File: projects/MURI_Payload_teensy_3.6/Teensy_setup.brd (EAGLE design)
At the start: 100 x 80 mm, 52 parts, among them IC1 DS18B20, IC2 DS18B20, IC4 DS18B20, IC5 DS18B20, U2 MS560702BA03-50

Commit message: Added edits to teensy 3.6 schematic for the plantower. Added stuff from EAGLE intro presentation.
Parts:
- added B1: SPARKFUN_LOGIC_LEVEL_CONVERTER, SparkFun-Boards:SPARKFUN_LOGIC_LEVEL_CONVERTER
- added PLANTOWER: (no value), SparkFun-Connectors:1X08
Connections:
- new net TX_PT_HIGH: B1.HV1, U$1.0/RX
- new net TX_PT_LOW: B1.LV1, PLANTOWER.4
- net 5V2: now also B1.HV
- net GND: now also B1.GND1, B1.GND2, PLANTOWER.2
- net VCC: now also B1.LV, PLANTOWER.1
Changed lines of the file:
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@@
 <attribute name="VALUE" x="-81.6356" y="-9.3726" size="0.9906" layer="27" ratio="10"/>
+</element>
+<element name="B1" library="SparkFun-Boards" library_urn="urn:adsk.eagle:library:509" package="SPARKFUN_LOGIC_LEVEL_CONVERTER" package3d_urn="urn:adsk.eagle:package:37318/1" value="SPARKFUN_LOGIC_LEVEL_CONVERTER" x="-91.44" y="-1.27" smashed="yes">
+<attribute name="NAME" x="-91.44" y="6.604" size="0.6096" layer="25" font="vector" ratio="20" align="bottom-center"/>
+<attribute name="VALUE" x="-91.44" y="-9.144" size="0.6096" layer="25" font="vector" ratio="20" align="top-center"/>
+</element>
+<element name="PLANTOWER" library="SparkFun-Connectors" library_urn="urn:adsk.eagle:library:513" package="1X08" package3d_urn="urn:adsk.eagle:package:38138/1" value="" x="-96.52" y="-12.7" smashed="yes">
+<attribute name="NAME" x="-97.79" y="-11.303" size="0.6096" layer="25" font="vector" ratio="20"/>
+<attribute name="PROD_ID" value="CONN-08438" x="-96.52" y="-12.7" size="1.778" layer="27" display="off"/>
+<attribute name="VALUE" x="-97.79" y="-14.732" size="0.6096" layer="27" font="vector" ratio="20"/>
 </element>
 </elements>
@@
 <contactref element="UBLOX" pad="4"/>
 <contactref element="XBEE" pad="4"/>
+<contactref element="PLANTOWER" pad="2"/>
+<contactref element="B1" pad="GND1"/>
+<contactref element="B1" pad="GND2"/>
+<wire x1="-96.52" y1="-2.54" x2="-93.98" y2="-12.7" width="0" layer="19" extent="1-1"/>
+<wire x1="-86.36" y1="-2.54" x2="-96.52" y2="-2.54" width="0" layer="19" extent="1-1"/>
+<wire x1="-73.66" y1="2.54" x2="-86.36" y2="-2.54" width="0" layer="19" extent="1-1"/>
 <wire x1="-80.01" y1="24.13" x2="-73.66" y2="2.54" width="0" layer="19" extent="1-1"/>
 <wire x1="-71.12" y1="38.1" x2="-80.01" y2="24.13" width="0" layer="19" extent="1-1"/>
@@
 <contactref element="BATTERY_HEATER_RELAY" pad="6"/>
 <contactref element="BATTERY_HEATER_RELAY" pad="9"/>
+<contactref element="B1" pad="HV"/>
+<wire x1="-69.85" y1="21.6154" x2="-86.36" y2="0" width="0" layer="19" extent="1-1"/>
 <wire x1="-64.77" y1="26.6954" x2="-69.85" y2="21.6154" width="0" layer="19" extent="1-1"/>
 <wire x1="-57.15" y1="21.6154" x2="-64.77" y2="26.6954" width="0" layer="19" extent="1-1"/>
@@
 <contactref element="R11" pad="2"/>
 <contactref element="U2" pad="2"/>
+<contactref element="PLANTOWER" pad="1"/>
+<contactref element="B1" pad="LV"/>
+<wire x1="-96.52" y1="0" x2="-96.52" y2="-12.7" width="0" layer="19" extent="1-1"/>
+<wire x1="-76.2" y1="-8.89" x2="-96.52" y2="-12.7" width="0" layer="19" extent="1-1"/>
 <wire x1="-76.2" y1="-3.81" x2="-76.2" y2="-8.89" width="0" layer="19" extent="1-1"/>
 <wire x1="-68.58" y1="17.78" x2="-76.2" y2="-3.81" width="0" layer="19" extent="1-1"/>
@@
 <wire x1="-15.24" y1="17.78" x2="-50.8" y2="63.5" width="0" layer="19" extent="1-1"/>
 </signal>
+<signal name="TX_PT_HIGH">
+<contactref element="B1" pad="HV1"/>
+<contactref element="U$1" pad="0/RX"/>
+<wire x1="-71.12" y1="2.54" x2="-86.36" y2="5.08" width="0" layer="19" extent="1-1"/>
+</signal>
+<signal name="TX_PT_LOW">
+<contactref element="B1" pad="LV1"/>
+<contactref element="PLANTOWER" pad="4"/>
+<wire x1="-96.52" y1="5.08" x2="-88.9" y2="-12.7" width="0" layer="19" extent="1-1"/>
+</signal>
 </signals>

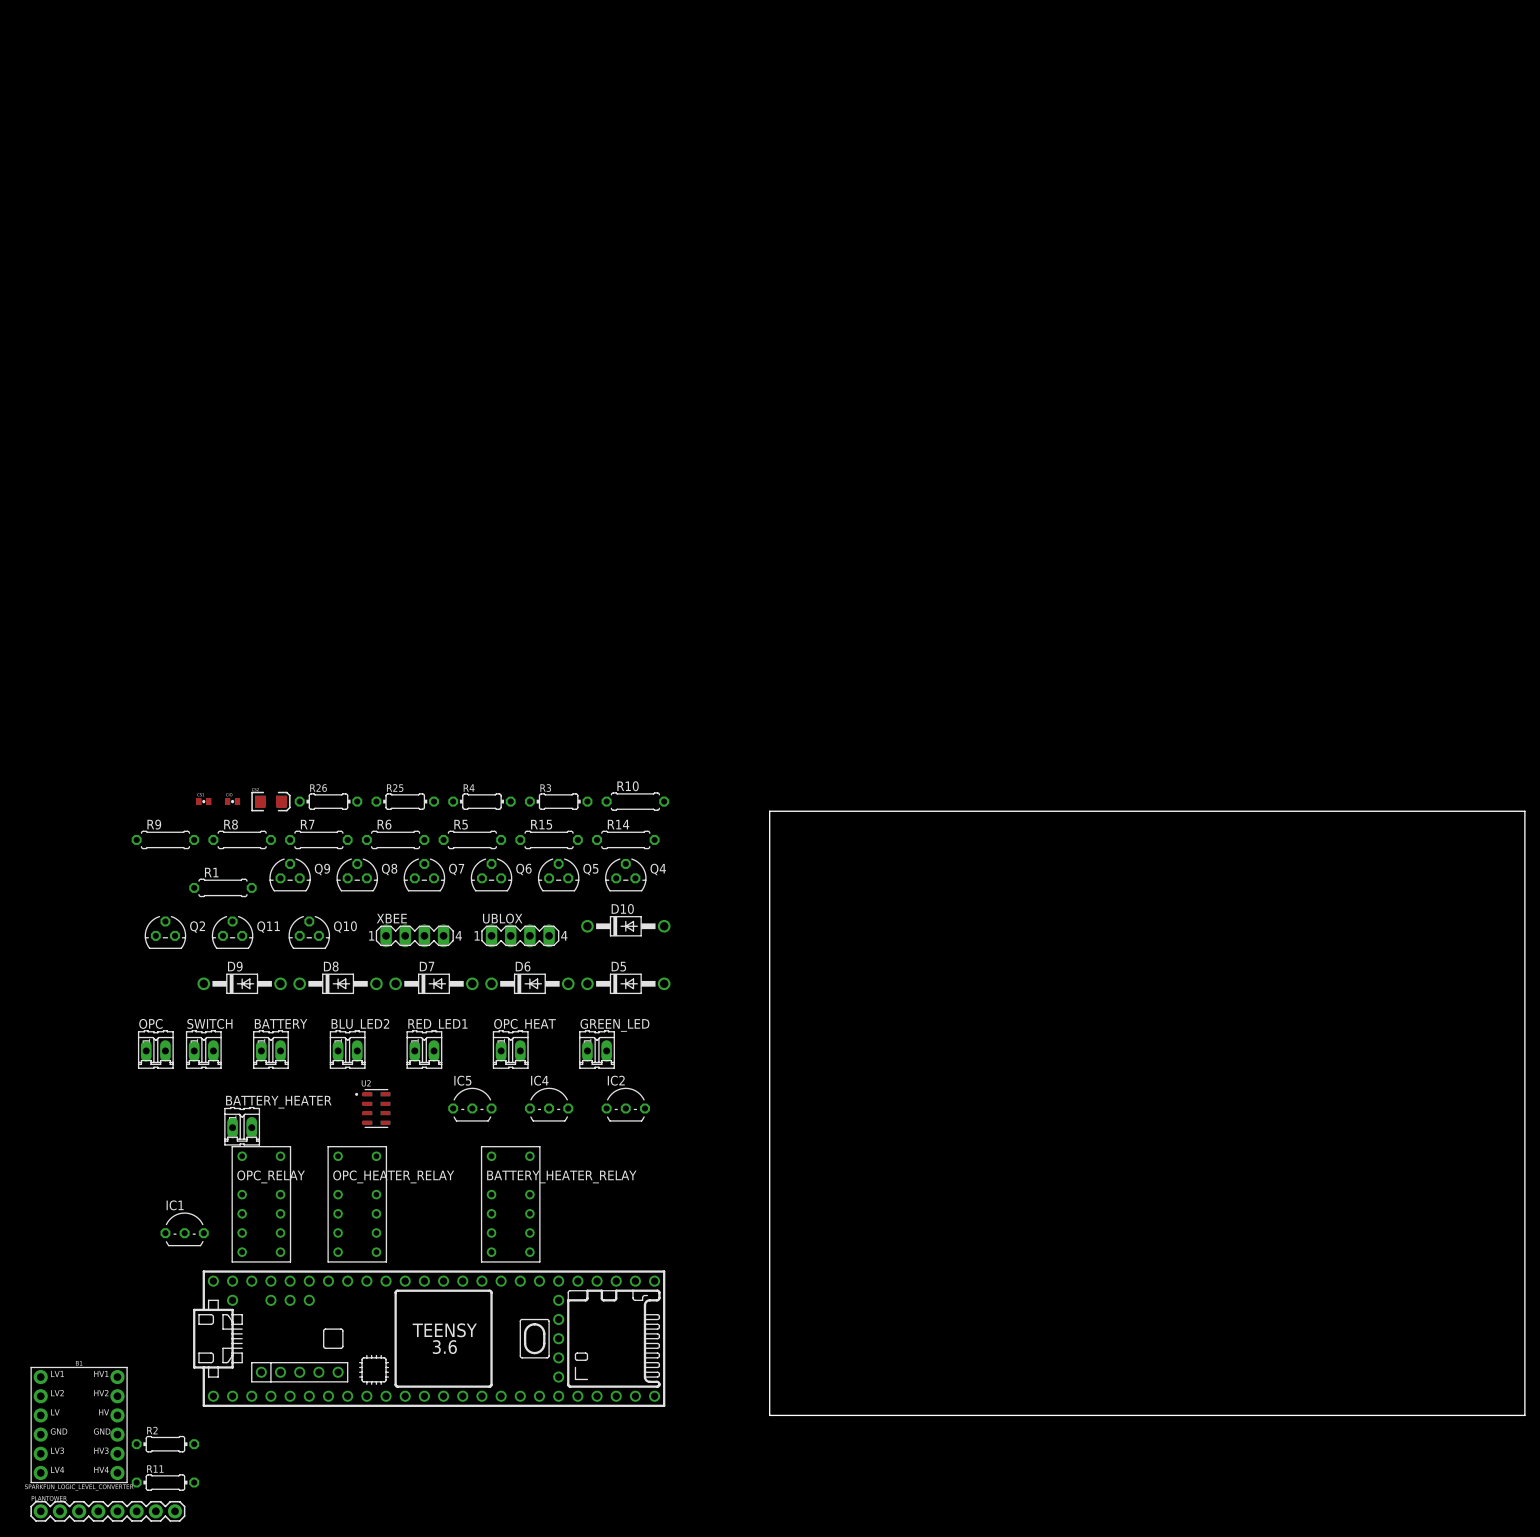
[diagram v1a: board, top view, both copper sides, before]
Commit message: I wired up the first iteration of the PCB and added terminal blocks to the schematic
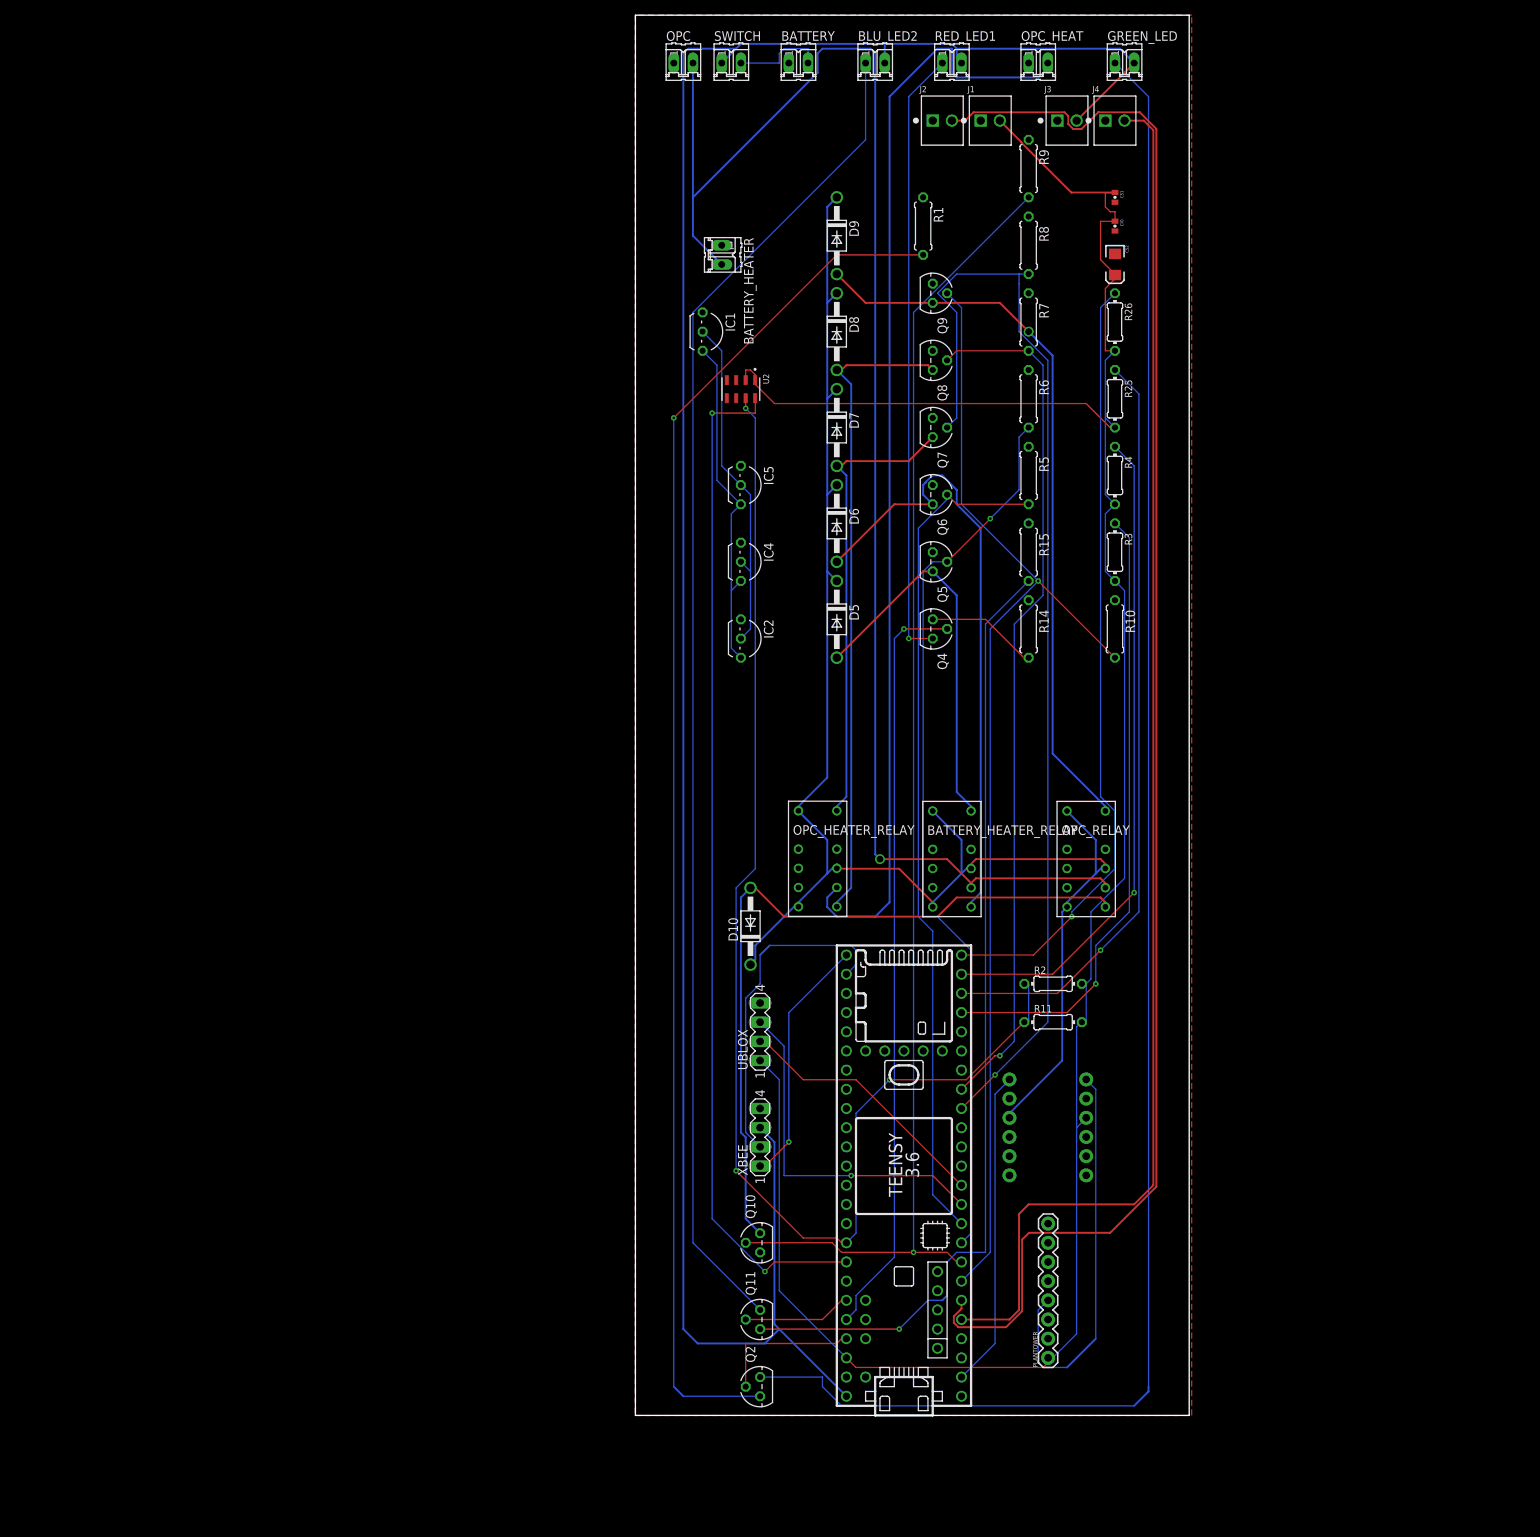
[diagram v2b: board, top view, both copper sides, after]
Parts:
- added J1, J2, J3, J4: 282834-2, 282834-2:CONN_282834-2
- moved BATTERY 148.3 mm to (3.81, 179.1)
- moved BLU_LED2 148.3 mm to (14.0, 179.1)
- moved SWITCH 148.3 mm to (-5.08, 179.1)
- moved GREEN_LED 148.3 mm to (47.0, 179.1)
- moved OPC 148.3 mm to (-11.4, 179.1)
- moved OPC_HEAT 148.3 mm to (35.6, 179.1)
- moved RED_LED1 148.3 mm to (24.1, 179.1)
- moved R9 144.8 mm to (34.3, 165.1), turned to 270 degrees
- moved CS1 144.8 mm to (45.7, 161.3), turned to 270 degrees
- moved CIO 139.5 mm to (45.7, 157.5), turned to 270 degrees
- moved IC1 137.7 mm to (-8.89, 143.5), turned to 270 degrees
- moved PLANTOWER 134.9 mm to (36.9, 7.62), turned to 90 degrees
- moved B1 134.2 mm to (36.8, 38.1), flipped to the bottom
- moved CS2 132.5 mm to (45.7, 152.4), turned to 270 degrees
- moved R11 132.4 mm to (37.5, 52.1)
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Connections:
- new net RX_3: J2.2, U$1.4/CANRX
- new net TX_3: J4.2, U$1.3/CANTX
- net 5V: now also J3.2
- net GND: now also J1.1, J2.1, J3.1, J4.1
- net VCC: now also J1.2
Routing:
- net VCC: track 0.00 -> 319.1 mm
- net 5V: track 0.00 -> 302.9 mm
- net N$5: track 0.00 -> 232.3 mm
- net 5V2: track 0.00 -> 222.0 mm
- net RX_3: track 0.00 -> 214.6 mm
- net OPC: track 0.00 -> 202.1 mm, vias 0 -> 1
- net TX_3: track 0.00 -> 184.2 mm
- net N$4: track 0.00 -> 182.2 mm, vias 0 -> 1
- net N$18: track 0.00 -> 178.3 mm
- net HV2: track 0.00 -> 175.6 mm, vias 0 -> 1
- net SDA: track 0.00 -> 173.6 mm, vias 0 -> 3
- net HV1: track 0.00 -> 154.4 mm, vias 0 -> 1
- net HV11: track 0.00 -> 149.3 mm, vias 0 -> 1
- net BATTERY_HEATER: track 0.00 -> 147.6 mm
- net SCL: track 0.00 -> 135.6 mm, vias 0 -> 2
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- added copper zone on layer 1, net GND
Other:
- board size 100 x 80 mm -> 73.3 x 185.4 mm
